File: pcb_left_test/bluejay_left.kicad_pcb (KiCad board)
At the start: 2 copper layers, 147 x 140.5 mm, 81 parts, among them J1 SJ-43514, U1 ATmega328P-PU, Y1 16MHz

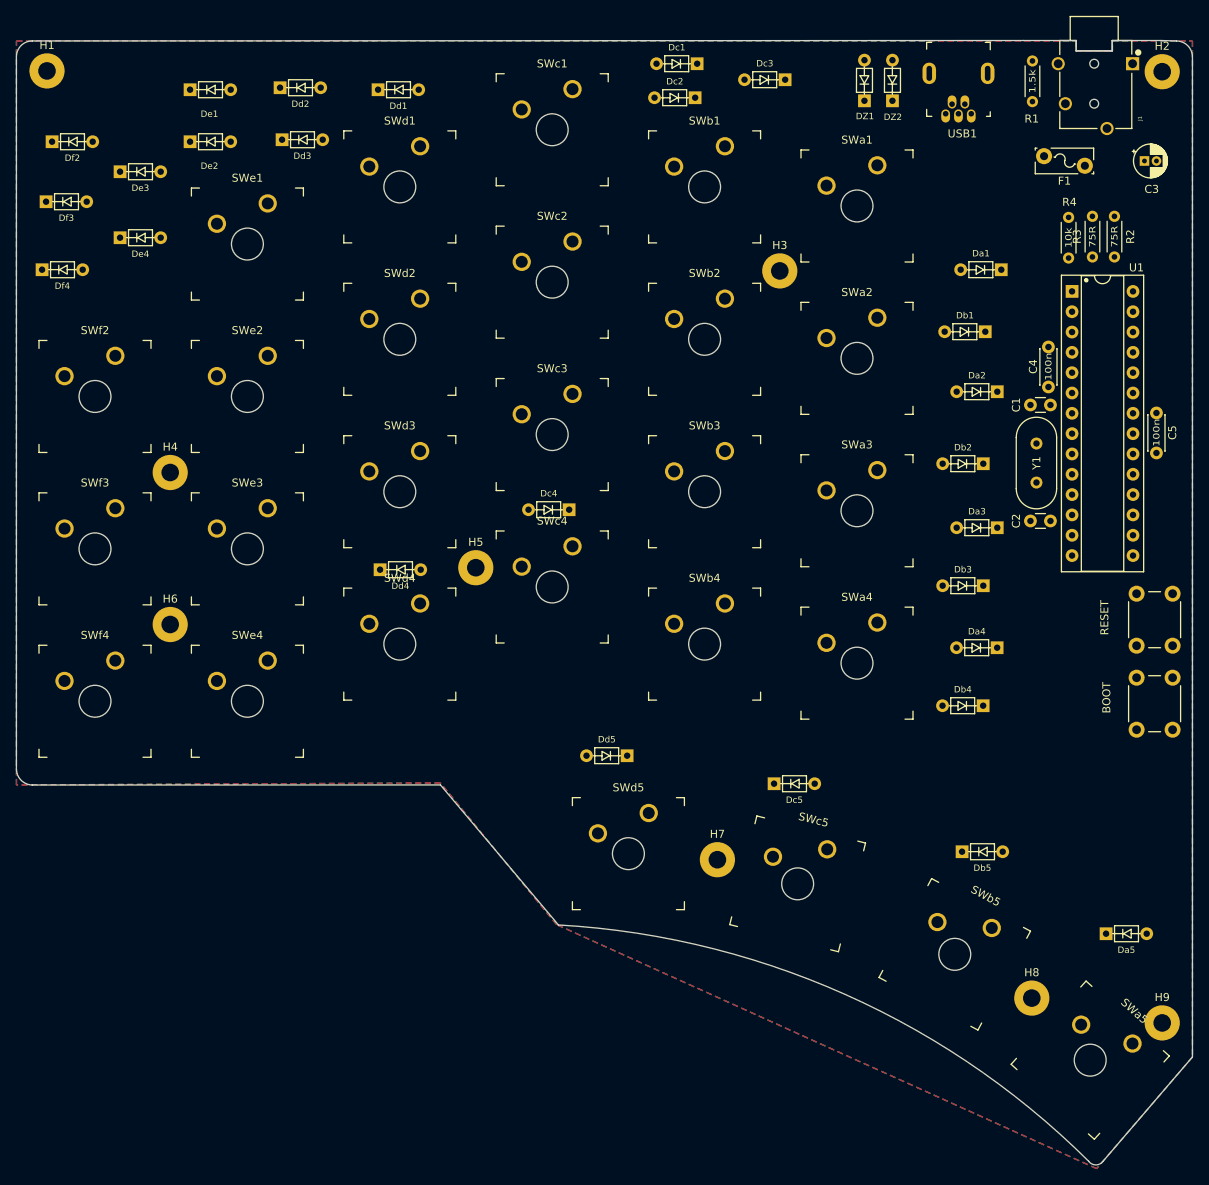
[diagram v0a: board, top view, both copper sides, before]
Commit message: Alternative approach to place diodes
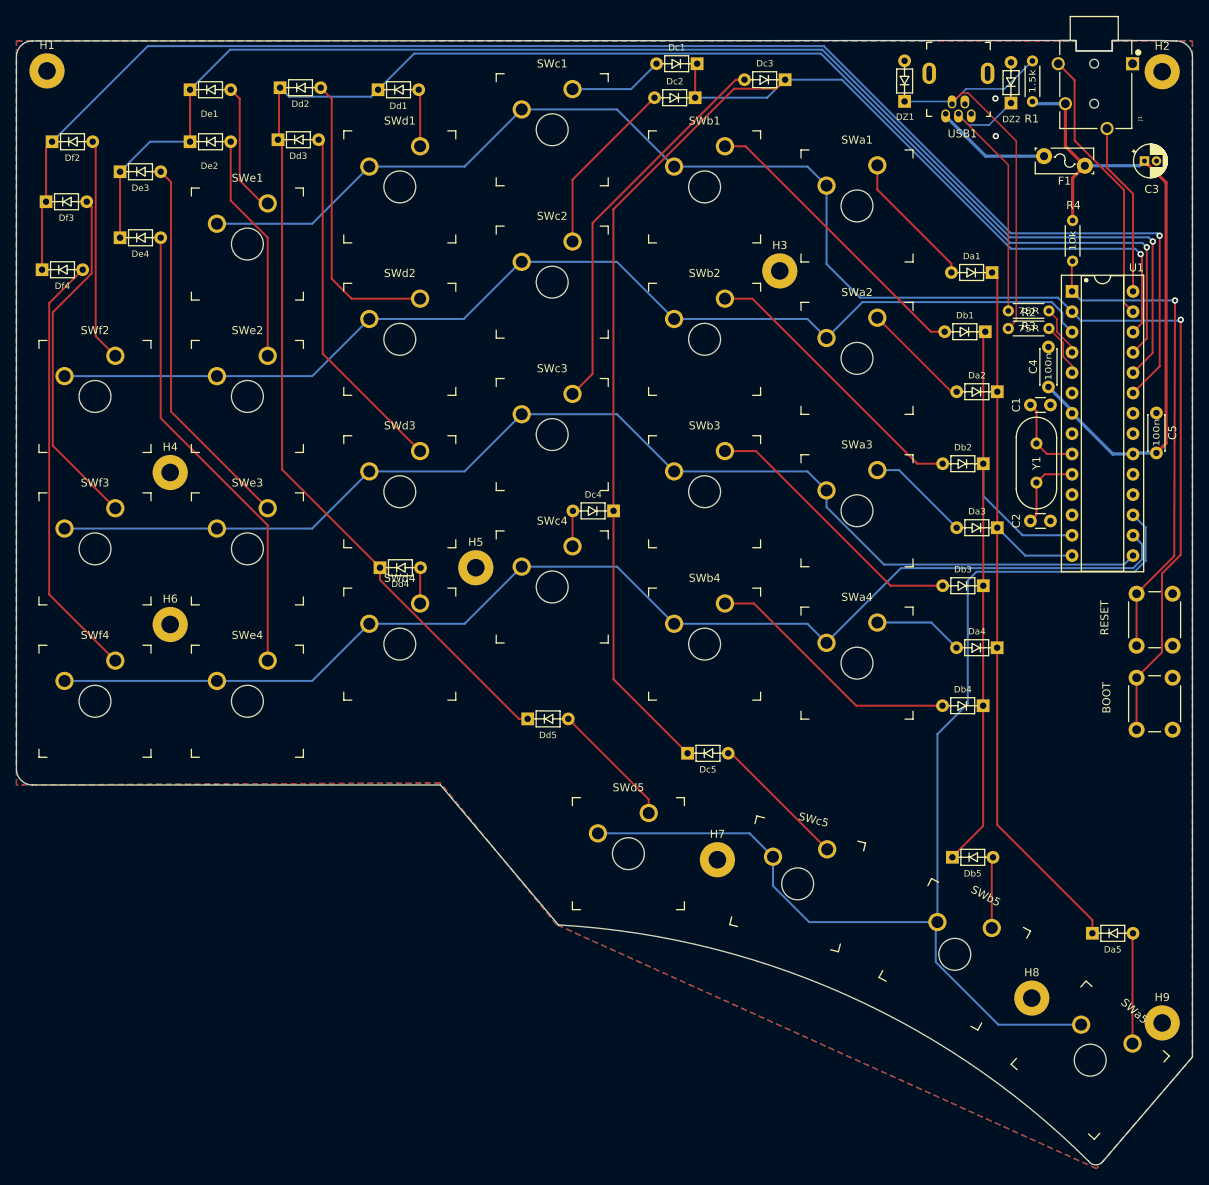
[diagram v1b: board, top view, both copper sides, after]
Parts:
- moved Dd5 15.7 mm to (-23.4, 28.4), turned to 0 degrees
- moved DZ2 14.8 mm to (38.3, -47.3)
- moved R2 12.1 mm to (43.0, -20.4), turned to 180 degrees
- moved Dc5 11.5 mm to (-3.40, 32.7)
- moved R3 8.67 mm to (43.0, -22.6), turned to 180 degrees
- moved Dc4 5.55 mm to (-10.1, 2.40)
- moved DZ1 5.02 mm to (25.0, -47.5)
- moved Da5 1.71 mm to (47.2, 55.2)
- moved Db5 1.40 mm to (29.7, 45.7)
- moved Da1 1.21 mm to (37.2, -27.4)
- moved R4 0.63 mm to (46.0, -33.9)
- moved Dd3 0.51 mm to (-54.6, -44.0)
- moved Dd4 0.25 mm to (-41.9, 9.50)
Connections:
- PB2 pad 1: /colD -> /row1
- U1 pad 11: /row3 -> unconnected-(U1-Pad11)
- U1 pad 12: /row4 -> unconnected-(U1-Pad12)
- U1 pad 13: /row5 -> /colB
- U1 pad 14: /colC -> /colA
- U1 pad 15: /colA -> /row3
- U1 pad 16: /colB -> /row4
- U1 pad 17: unconnected-(U1-Pad17) -> /row5
- U1 pad 2: /colD -> /row1
- U1 pad 23: unconnected-(U1-Pad23) -> /colF
- U1 pad 24: unconnected-(U1-Pad24) -> /colE
- U1 pad 25: /colE -> /colD
- U1 pad 26: /colF -> /colC
- U1 pad 3: /row1 -> /row2
- U1 pad 6: /row2 -> unconnected-(U1-Pad6)
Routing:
- net /colD: track 0.00 -> 227.5 mm, vias 0 -> 1
- net /row1: track 0.00 -> 196.7 mm, vias 0 -> 1
- net /colF: track 0.00 -> 190.8 mm, vias 0 -> 1
- net /colC: track 0.00 -> 180.3 mm, vias 0 -> 1
- net /colE: track 0.00 -> 174.8 mm, vias 0 -> 1
- net /row4: track 0.00 -> 152.4 mm
- net /row5: track 0.00 -> 149.6 mm
- net /row3: track 0.00 -> 148.9 mm
- net /row2: track 0.00 -> 139.9 mm
- net /colA: track 0.00 -> 98.6 mm
- net /colB: track 0.00 -> 84.6 mm
- net VCC: track 0.00 -> 83.5 mm
- net Net-(PB1-Pad1): track 0.00 -> 62.3 mm, vias 0 -> 1
- net Net-(De4-Pad2): track 0.00 -> 58.4 mm
- net Net-(Df4-Pad2): track 0.00 -> 54.0 mm
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
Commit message: Fine tune placement of diodes
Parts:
- moved Dc1 7.19 mm to (7.45, -52.5)
- moved Dc3 4.59 mm to (14.9, -48.6)
- moved Db5 3.63 mm to (32.7, 43.6)
- moved Dc4 2.61 mm to (-7.50, 2.40)
- moved Dd1 2.25 mm to (-42.1, -52.5)
- moved Df2 1.69 mm to (-81.7, -45.0)
- moved De4 0.76 mm to (-75.0, -32.0)
- moved Dc2 0.71 mm to (-0.20, -48.6)
- moved Df3 0.69 mm to (-82.9, -36.2)
- moved De3 0.66 mm to (-73.8, -40.5)
- moved R1 0.09 mm to (41.0, -53.8)
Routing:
- net Net-(Dc1-Pad2): track 11.8 -> 18.5 mm
- net /colB: track 84.6 -> 81.3 mm
- net Net-(Db5-Pad2): track 8.90 -> 12.2 mm
- net /colC: track 180.3 -> 177.5 mm
- net Net-(Dd1-Pad2): track 7.14 -> 9.40 mm
- net Net-(Dc3-Pad2): track 48.8 -> 51.0 mm
- net Net-(Dc4-Pad2): track 4.45 -> 5.53 mm
- net /colD: track 227.5 -> 228.3 mm
- net Net-(Dc2-Pad2): track 22.2 -> 21.5 mm
- net Net-(Df2-Pad2): track 27.9 -> 28.6 mm
- net Net-(De4-Pad2): track 58.4 -> 59.0 mm
